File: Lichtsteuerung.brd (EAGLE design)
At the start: 157.7 x 86.4 mm, 132 parts, among them IC1 74HC595D, IC10 TSR_1-2450, IC11 MEGA64-A, IC12 75176AD, IC13 DS1307SO8, IC2 74HC595D, IC3 74HC595D, IC4 74HC595D, IC5 75176AD, IC6 MEGA8-AI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

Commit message: RZL-Logo muss sein.
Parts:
- added U$1: (no value), RaumZeitLabor:RAUMZEITLABOR_-_LOGO_-_SCHWARZ
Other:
- board text added: "RaumZeitLabor Lichtsteuerung Rev. A"
- board text removed: "RaumZeitLabor Lichtsteuerung Board Rev. A"
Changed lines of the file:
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@@
 <setting verticaltext="up"/>
 </settings>
-<grid distance="137.795276" unitdist="mil" unit="mil" style="lines" multiple="1" display="yes" altdistance="0.35" altunitdist="mm" altunit="mm"/>
+<grid distance="0.003125" unitdist="mic" unit="mm" style="lines" multiple="1" display="yes" altdistance="0.35" altunitdist="mm" altunit="mm"/>
 <layers>
 <layer number="1" name="Top" color="4" fill="1" visible="yes" active="yes"/>
@@
 <layer number="38" name="bTest" color="7" fill="1" visible="no" active="yes"/>
 <layer number="39" name="tKeepout" color="4" fill="11" visible="yes" active="yes"/>
-<layer number="40" name="bKeepout" color="1" fill="11" visible="yes" active="yes"/>
+<layer number="40" name="bKeepout" color="1" fill="11" visible="no" active="yes"/>
 <layer number="41" name="tRestrict" color="4" fill="10" visible="yes" active="yes"/>
-<layer number="42" name="bRestrict" color="1" fill="10" visible="yes" active="yes"/>
+<layer number="42" name="bRestrict" color="1" fill="10" visible="no" active="yes"/>
 <layer number="43" name="vRestrict" color="2" fill="10" visible="yes" active="yes"/>
 <layer number="44" name="Drills" color="7" fill="1" visible="no" active="yes"/>
@@
 <layer number="50" name="dxf" color="14" fill="1" visible="yes" active="yes"/>
 <layer number="51" name="tDocu" color="7" fill="1" visible="no" active="yes"/>
-<layer number="52" name="bDocu" color="7" fill="1" visible="yes" active="yes"/>
+<layer number="52" name="bDocu" color="7" fill="1" visible="no" active="yes"/>
 <layer number="53" name="tGND_GNDA" color="7" fill="9" visible="no" active="no"/>
 <layer number="54" name="bGND_GNDA" color="1" fill="9" visible="no" active="no"/>
@@
 <text x="129.54" y="84.7725" size="1.016" layer="25" rot="R180">ISP MAIN</text>
 <text x="151.13" y="84.7725" size="1.016" layer="25" rot="R180">ISP DMX OUT</text>
-<text x="154.94" y="19.05" size="1.778" layer="25" rot="R90">RaumZeitLabor Lichtsteuerung Board Rev. A</text>
+<text x="154.94" y="19.05" size="1.778" layer="25" rot="R90">RaumZeitLabor Lichtsteuerung Rev. A</text>
 <text x="15.875" y="76.2" size="1.016" layer="25" rot="R270">DMX IN A</text>
 <text x="4.445" y="76.2" size="1.016" layer="25" rot="R270">DMX OUT A</text>
@@
 <text x="36.5125" y="76.2" size="1.016" layer="25" rot="R270">+24V</text>
 <text x="39.0525" y="76.2" size="1.016" layer="25" rot="R270">+24V</text>
-<wire x1="6.35" y1="83.82" x2="6.35" y2="67.31" width="0.4064" layer="25"/>
-<wire x1="8.89" y1="83.82" x2="8.89" y2="67.31" width="0.4064" layer="25"/>
-<wire x1="17.78" y1="83.82" x2="17.78" y2="67.31" width="0.4064" layer="25"/>
-<wire x1="20.32" y1="83.82" x2="20.32" y2="67.31" width="0.4064" layer="25"/>
-<wire x1="29.21" y1="83.82" x2="29.21" y2="67.31" width="0.4064" layer="25"/>
-<wire x1="38.1" y1="83.82" x2="38.1" y2="67.31" width="0.4064" layer="25"/>
-<wire x1="40.64" y1="83.82" x2="40.64" y2="67.31" width="0.4064" layer="25"/>
-<wire x1="43.18" y1="83.82" x2="43.18" y2="67.31" width="0.4064" layer="25"/>
+<wire x1="6.35" y1="83.82" x2="6.35" y2="70.81" width="0.4064" layer="25"/>
+<wire x1="8.89" y1="83.82" x2="8.89" y2="70.81" width="0.4064" layer="25"/>
+<wire x1="17.78" y1="83.82" x2="17.78" y2="70.81" width="0.4064" layer="25"/>
+<wire x1="20.32" y1="83.82" x2="20.32" y2="70.81" width="0.4064" layer="25"/>
+<wire x1="29.21" y1="83.82" x2="29.21" y2="70.81" width="0.4064" layer="25"/>
+<wire x1="38.1" y1="83.82" x2="38.1" y2="70.81" width="0.4064" layer="25"/>
+<wire x1="40.64" y1="83.82" x2="40.64" y2="70.81" width="0.4064" layer="25"/>
+<wire x1="43.18" y1="83.82" x2="43.18" y2="70.81" width="0.4064" layer="25"/>
 <text x="38.735" y="17.145" size="1.016" layer="25">+24V</text>
 <text x="10.4775" y="17.145" size="1.016" layer="25">1</text>
@@
 <attribute name="VALUE" x="47.625" y="44.45" size="1.27" layer="27" rot="R270"/>
 </element>
+<element name="U$1" library="RaumZeitLabor" package="RAUMZEITLABOR_-_LOGO_-_SCHWARZ" value="" x="113.4" y="47.95"/>
 </elements>
 <signals>

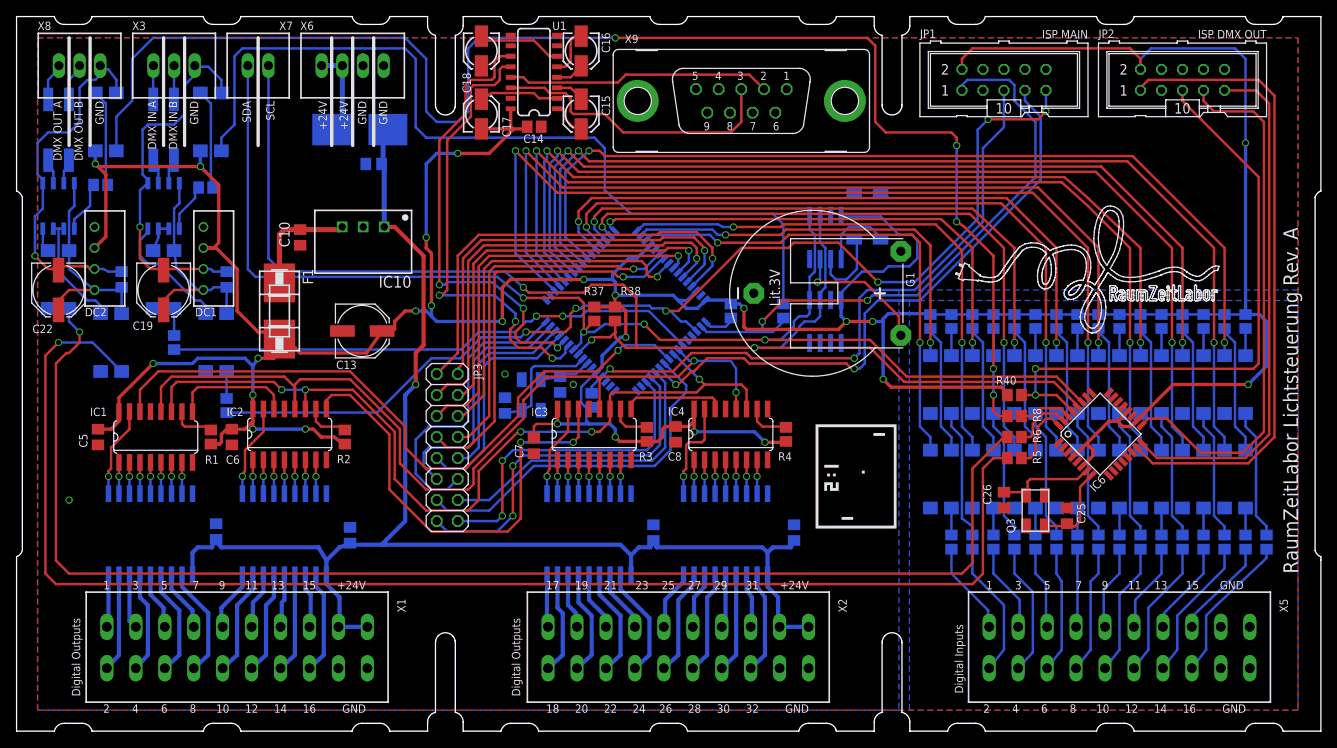
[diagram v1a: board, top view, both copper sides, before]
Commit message: Added polyfuses for the 24V rails
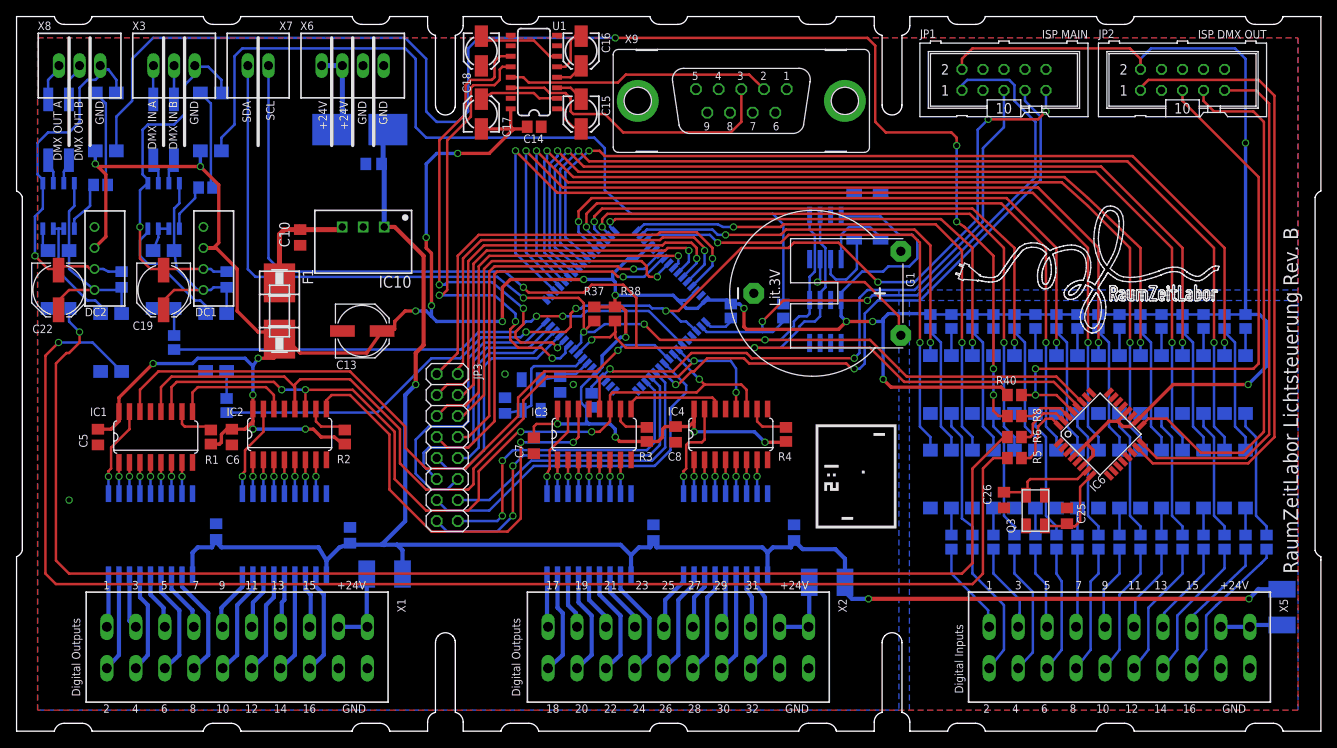
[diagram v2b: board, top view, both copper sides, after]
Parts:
- added F3, F4, F5: 500mA, ptc-littlefuse:1812L
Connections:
- new net +24V_01: F3.P$1, X1.L17, X1.L19
- new net +24V_02: F4.P$2, X2.L17, X2.L19
- new net +24V_03: F5.P$2, X5.L17, X5.L19
- net +24V: now also F3.P$2, F4.P$1, F5.P$1; no longer X1.L17, X1.L19, X2.L17, X2.L19
- net GNDINT: no longer X5.L17, X5.L19
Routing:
- net +24V: track 165.2 -> 213.0 mm, vias 1 -> 3
- net +24V_01: track 0.00 -> 9.92 mm
- net +24V_02: track 0.00 -> 8.92 mm
- net +24V_03: track 0.00 -> 7.50 mm
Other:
- board text added: "RaumZeitLabor Lichtsteuerung Rev. B"
- board text removed: "RaumZeitLabor Lichtsteuerung Rev. A"
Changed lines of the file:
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@@
 <setting verticaltext="up"/>
 </settings>
-<grid distance="0.003125" unitdist="mic" unit="mm" style="lines" multiple="1" display="yes" altdistance="0.35" altunitdist="mm" altunit="mm"/>
+<grid distance="39.3700787" unitdist="mil" unit="mil" style="lines" multiple="1" display="yes" altdistance="0.5" altunitdist="mm" altunit="mm"/>
 <layers>
 <layer number="1" name="Top" color="4" fill="1" visible="yes" active="yes"/>
@@
 <text x="129.54" y="84.7725" size="1.016" layer="25" rot="R180">ISP MAIN</text>
 <text x="151.13" y="84.7725" size="1.016" layer="25" rot="R180">ISP DMX OUT</text>
-<text x="154.94" y="19.05" size="1.778" layer="25" rot="R90">RaumZeitLabor Lichtsteuerung Rev. A</text>
+<text x="154.94" y="19.05" size="1.778" layer="25" rot="R90">RaumZeitLabor Lichtsteuerung Rev. B</text>
 <text x="15.875" y="76.2" size="1.016" layer="25" rot="R270">DMX IN A</text>
 <text x="4.445" y="76.2" size="1.016" layer="25" rot="R270">DMX OUT A</text>
@@
 <text x="84.3475" y="17.145" size="1.016" layer="25">29</text>
 <text x="88.1575" y="17.145" size="1.016" layer="25">31</text>
-<text x="145.485" y="17.145" size="1.016" layer="25">GND</text>
+<text x="145.485" y="17.145" size="1.016" layer="25">+24V</text>
 <text x="117.2275" y="17.145" size="1.016" layer="25">1</text>
 <text x="120.72" y="17.145" size="1.016" layer="25">3</text>
@@
 </element>
 <element name="U$1" library="RaumZeitLabor" package="RAUMZEITLABOR_-_LOGO_-_SCHWARZ" value="" x="113.4" y="47.95"/>
+<element name="F3" library="ptc-littlefuse" package="1812L" value="500mA" x="44.5" y="19" rot="MR180"/>
+<element name="F4" library="ptc-littlefuse" package="1812L" value="500mA" x="98" y="18" rot="MR0"/>
+<element name="F5" library="ptc-littlefuse" package="1812L" value="500mA" x="153" y="15" rot="MR270"/>
 </elements>
 <signals>
@@
 <contactref element="ULN4" pad="10"/>
 <contactref element="C4" pad="1"/>
-<contactref element="X1" pad="L19"/>
-<contactref element="X1" pad="L17"/>
-<contactref element="X2" pad="L19"/>
-<contactref element="X2" pad="L17"/>
 <contactref element="F2" pad="P$1"/>
 <wire x1="44.45" y1="68.63" x2="44.13" y2="68.58" width="0.6096" layer="16"/>
@@
 <wire x1="36.5125" y1="22.225" x2="37.465" y2="20.6375" width="0.508" layer="16"/>
 <wire x1="37.465" y1="20.6375" x2="37.465" y2="18.9103" width="0.508" layer="16"/>
-<wire x1="37.465" y1="18.9103" x2="37.465" y2="17.78" width="0.508" layer="16"/>
-<wire x1="37.465" y1="17.78" x2="39.0525" y2="16.1925" width="0.508" layer="16"/>
-<wire x1="39.0525" y1="16.1925" x2="39.0525" y2="12.7425" width="0.508" layer="16"/>
-<wire x1="39.0525" y1="12.7425" x2="38.92" y2="12.61" width="0.508" layer="16"/>
-<wire x1="38.92" y1="12.61" x2="42.42" y2="12.61" width="0.508" layer="16"/>
 <wire x1="37.465" y1="20.6375" x2="39.0525" y2="22.225" width="0.508" layer="16"/>
 <wire x1="39.0525" y1="22.225" x2="39.9425" y2="22.5425" width="0.508" layer="16"/>
@@
 <wire x1="91.44" y1="22.225" x2="93.625" y2="22.225" width="0.508" layer="16"/>
 <wire x1="93.625" y1="22.225" x2="94" y2="23.05" width="0.508" layer="16"/>
-<wire x1="90.805" y1="18.9103" x2="90.805" y2="17.4625" width="0.508" layer="16"/>
-<wire x1="90.805" y1="17.4625" x2="92.075" y2="16.1925" width="0.508" layer="16"/>
-<wire x1="92.075" y1="16.1925" x2="92.075" y2="12.795" width="0.508" layer="16"/>
-<wire x1="92.075" y1="12.795" x2="92.26" y2="12.61" width="0.508" layer="16"/>
-<wire x1="92.26" y1="12.61" x2="95.76" y2="12.61" width="0.508" layer="16"/>
 <wire x1="74.295" y1="18.9103" x2="74.295" y2="21.2725" width="0.508" layer="16"/>
 <wire x1="74.295" y1="21.2725" x2="73.025" y2="22.5425" width="0.508" layer="16"/>
-<wire x1="73.025" y1="22.5425" x2="44.45" y2="22.5425" width="0.508" layer="16"/>
+<wire x1="73.025" y1="22.5425" x2="46" y2="22.5425" width="0.508" layer="16"/>
+<wire x1="46" y1="22.5425" x2="44.45" y2="22.5425" width="0.508" layer="16"/>
 <wire x1="44.45" y1="22.5425" x2="40.64" y2="22.5425" width="0.508" layer="16"/>
 <wire x1="40.64" y1="22.5425" x2="40.3175" y2="22.7325" width="0.508" layer="16"/>
@@
 <wire x1="44.31" y1="72.14" x2="44.31" y2="68.76" width="0.6096" layer="16"/>
 <wire x1="44.31" y1="68.76" x2="44.13" y2="68.58" width="0.6096" layer="16"/>
+<contactref element="F5" pad="P$1"/>
+<contactref element="F4" pad="P$1"/>
+<contactref element="F3" pad="P$2"/>
+<wire x1="46.66" y1="19" x2="46.66" y2="21.8825" width="0.508" layer="16"/>
+<wire x1="46.66" y1="21.8825" x2="46" y2="22.5425" width="0.508" layer="16"/>
+<wire x1="100.16" y1="18" x2="100.16" y2="20.84" width="0.508" layer="16"/>
+<wire x1="100.16" y1="20.84" x2="99" y2="22" width="0.508" layer="16"/>
+<wire x1="99" y1="22" x2="95.05" y2="22" width="0.508" layer="16"/>
+<wire x1="95.05" y1="22" x2="94" y2="23.05" width="0.508" layer="16"/>
+<wire x1="153" y1="17.16" x2="150.16" y2="17.16" width="0.508" layer="16"/>
+<wire x1="150.16" y1="17.16" x2="150" y2="17" width="0.6096" layer="16"/>
+<wire x1="150" y1="17" x2="149" y2="16" width="0.508" layer="16"/>
+<via x="149" y="16" extent="1-16" drill="0.6" shape="square"/>
+<wire x1="149" y1="16" x2="103" y2="16" width="0.508" layer="1"/>
+<via x="103" y="16" extent="1-16" drill="0.6" shape="square"/>
+<wire x1="103" y1="16" x2="101" y2="16" width="0.508" layer="16"/>
+<wire x1="101" y1="16" x2="100" y2="17" width="0.508" layer="16"/>
+<wire x1="100" y1="17" x2="100" y2="17.84" width="0.6096" layer="16"/>
+<wire x1="100" y1="17.84" x2="100.16" y2="18" width="0.6096" layer="16"/>
 </signal>
 <signal name="N$37">
@@
 <contactref element="OK115" pad="2"/>
 <contactref element="OK116" pad="2"/>
-<contactref element="X5" pad="L19"/>
-<contactref element="X5" pad="L17"/>
 <contactref element="X5" pad="L20"/>
 <contactref element="X5" pad="L18"/>
@@
 <contactref element="IC11" pad="43"/>
 </signal>
+<signal name="+24V_01" class="1">
+<contactref element="X1" pad="L19"/>
+<contactref element="X1" pad="L17"/>
+<contactref element="F3" pad="P$1"/>
+<wire x1="38.92" y1="12.61" x2="42.42" y2="12.61" width="0.508" layer="16"/>
+<wire x1="42.34" y1="19" x2="42.34" y2="12.69" width="0.508" layer="16"/>
+<wire x1="42.34" y1="12.69" x2="42.42" y2="12.61" width="0.508" layer="16"/>
+</signal>
+<signal name="+24V_02" class="1">
+<contactref element="X2" pad="L19"/>
+<contactref element="X2" pad="L17"/>
+<contactref element="F4" pad="P$2"/>
+<wire x1="92.26" y1="12.61" x2="95.76" y2="12.61" width="0.508" layer="16"/>
+<wire x1="95.84" y1="18" x2="95.84" y2="12.69" width="0.508" layer="16"/>
+<wire x1="95.84" y1="12.69" x2="95.76" y2="12.61" width="0.508" layer="16"/>
+</signal>
+<signal name="+24V_03" class="1">
+<contactref element="X5" pad="L19"/>
+<contactref element="X5" pad="L17"/>
+<contactref element="F5" pad="P$2"/>
+<wire x1="145.6" y1="12.61" x2="149.1" y2="12.61" width="0.508" layer="16"/>
+<wire x1="153" y1="12.84" x2="149.33" y2="12.84" width="0.508" layer="16"/>
+<wire x1="149.33" y1="12.84" x2="149.1" y2="12.61" width="0.508" layer="16"/>
+</signal>
 </signals>
